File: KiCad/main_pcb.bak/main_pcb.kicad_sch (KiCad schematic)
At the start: 19 parts, among them J3 1x6 Header

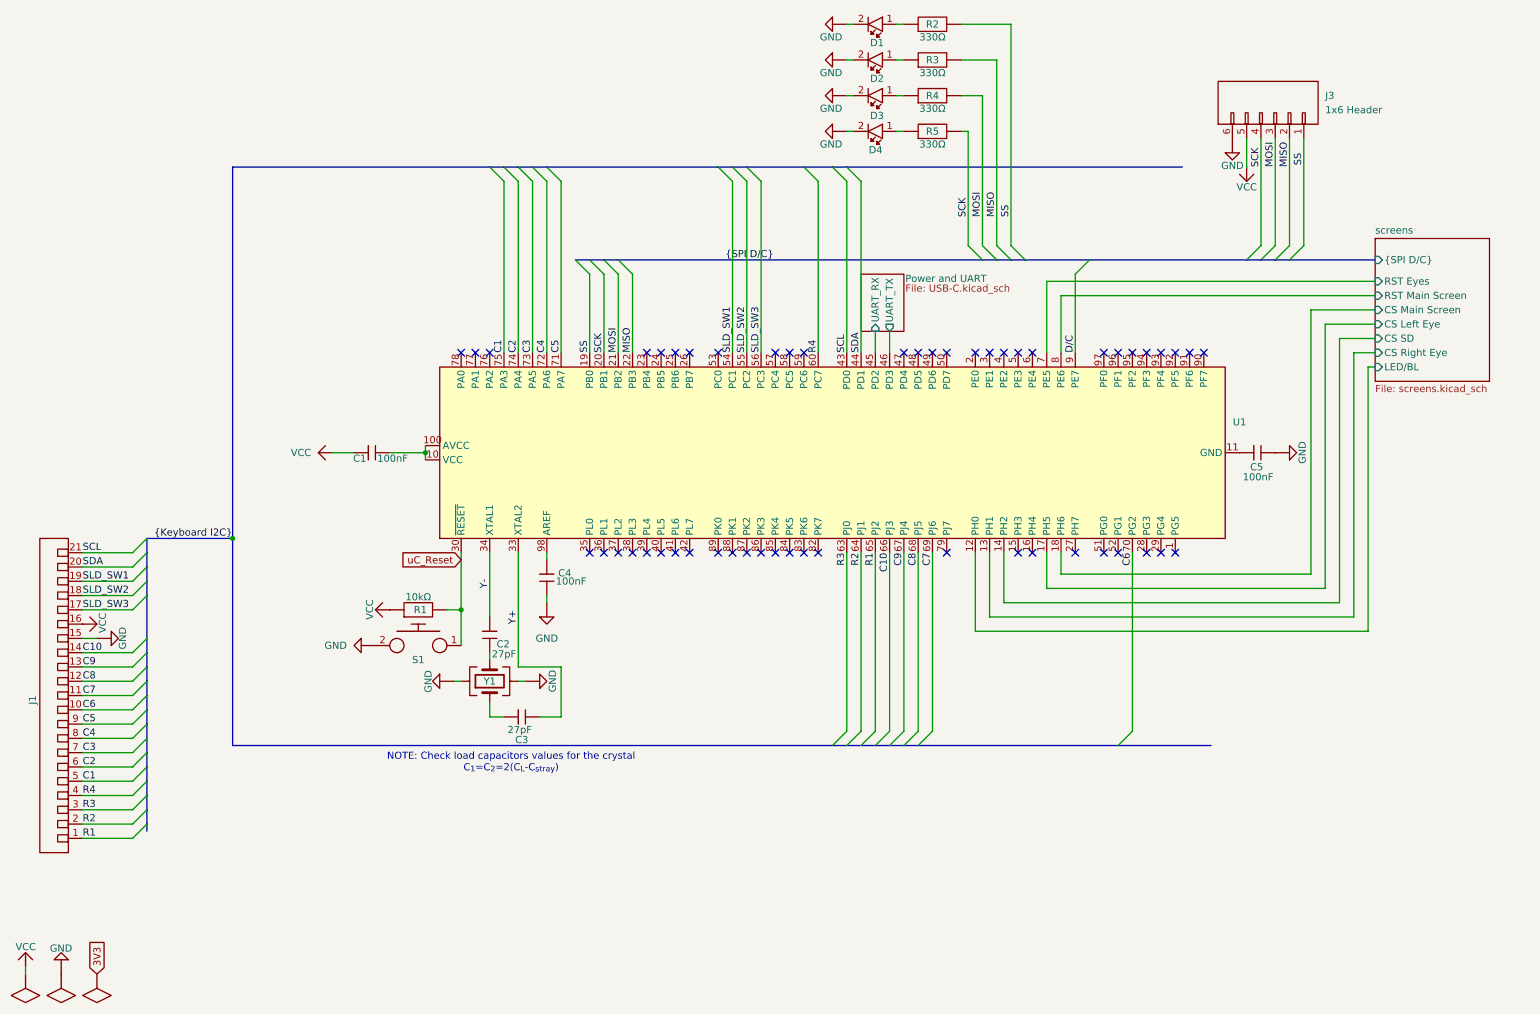
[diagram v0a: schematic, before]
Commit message: chore(migration): Puts old layout in main_pcb.bak/ and new layout to main_pcb/
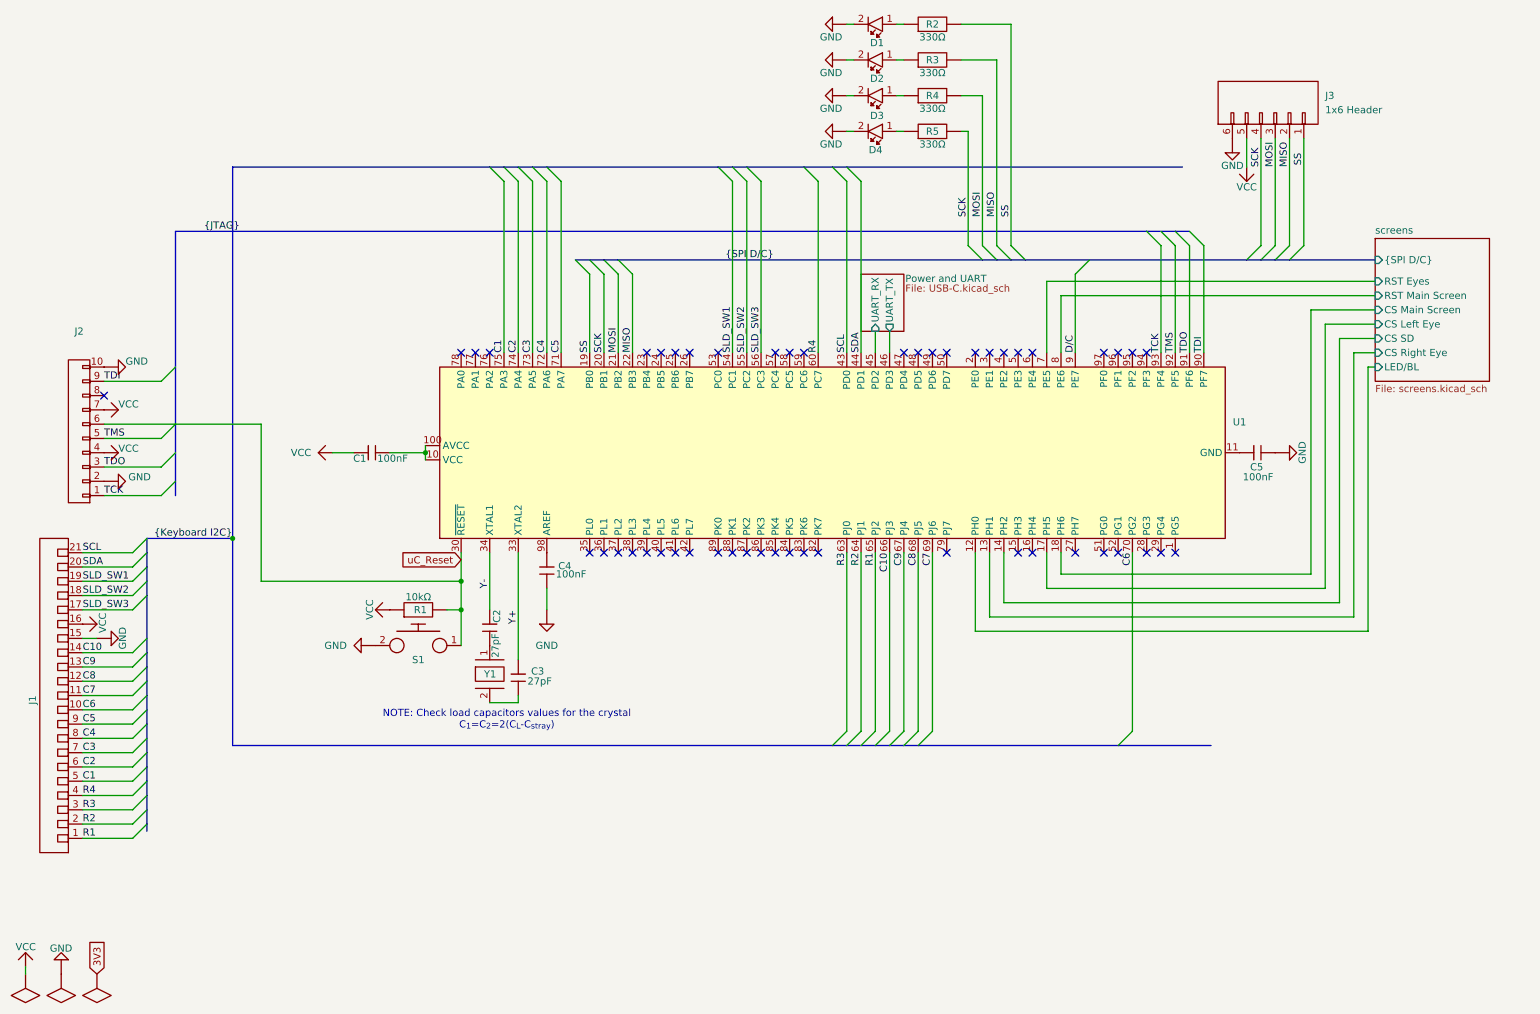
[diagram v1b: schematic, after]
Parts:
- added J2: ~, Connector_JST:JST_XH_B10B-XH-A_1x10_P2.50mm_Vertical, symbol Lily's Pad:2X5_Header
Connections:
- net GND: now also J2.10, J2.2; no longer Y1.2 (G), Y1.4 (G)
- net VCC: now also J2.4, J2.7
- net Y+: now also C3.1; no longer C3.2
- net uC_Reset: now also J2.6
- net at Y1.1: now also C2.2; no longer C3.1
- net TDI: now reaches U1.90 (PF7)
- net TDI: now also J2.9
- net TDO: now reaches U1.91 (PF6)
- net TDO: now also J2.3
- net TMS: now reaches U1.92 (PF5)
- net TMS: now also J2.5
- net TCK: now reaches U1.93 (PF4)
- net TCK: now also J2.1
- new net: C3.2, Y1.2
- no-connect marks 53 -> 50
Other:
- moved on the sheet: C2, C3, C4
